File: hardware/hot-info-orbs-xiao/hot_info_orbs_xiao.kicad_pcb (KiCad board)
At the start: 2 copper layers, 198.8 x 45.8 mm, 13 parts, among them SW1 SW_Push, SW2 SW_Push, SW3 SW_Push, U2 XIAO ESP32-S3 Plus

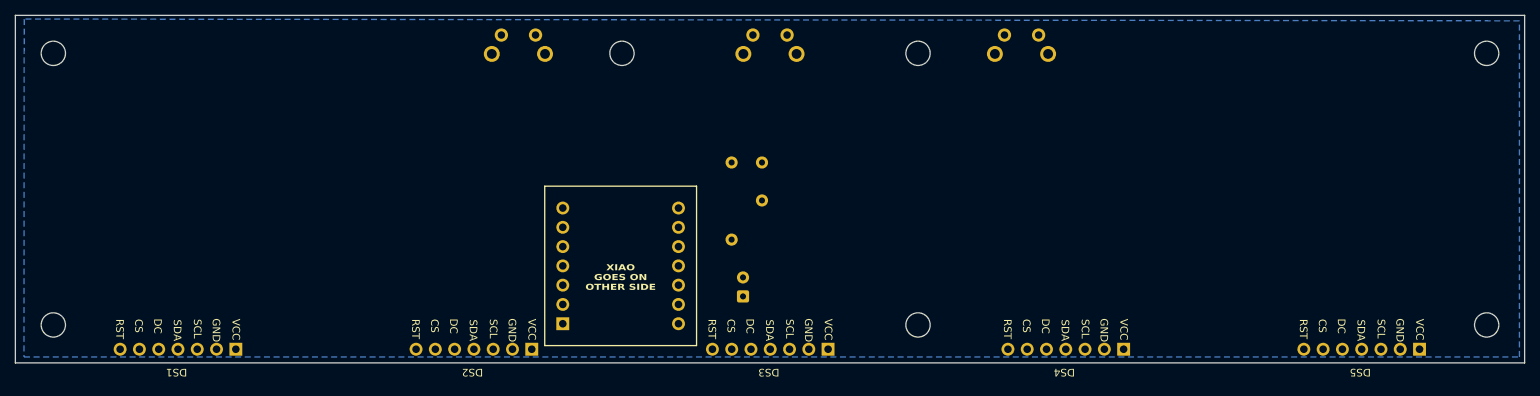
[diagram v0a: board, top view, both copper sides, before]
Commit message: xiao: routed - bottom edge 2 mm lower, 0 errors / 0 unconnected
Freerouting left one connection on every run (SCLK, or DC DS4->DS5) with
the display pin rows 1.8 mm from the bottom edge: nothing could pass under
them. Scott offered a couple of mm at the bottom; 2 mm routes clean in one
pass. Pin rows, parts and holes stay put (bottom holes now 7 mm in).

Rejected first, cheaper but failed:
- GND left to the B.Cu pour instead of tracks: everything else routes, but
  the tracks slice the pour and 6 GND pads end up islanded.
- Reordering nets in the DSN: 12 shuffles, identical result.

route_xiao.py: hole keepouts grown 0.4 mm (two copper_edge_clearance
errors otherwise), and an empty SES is rerun instead of read as "unrouted" -
it is an exit race (docs/TRAPS.md).

DRC with refilled zones: 0 errors, 0 warnings, 0 unconnected, 0 parity.

Co-Authored-By: Claude Opus 5.5 <noreply@anthropic.com>
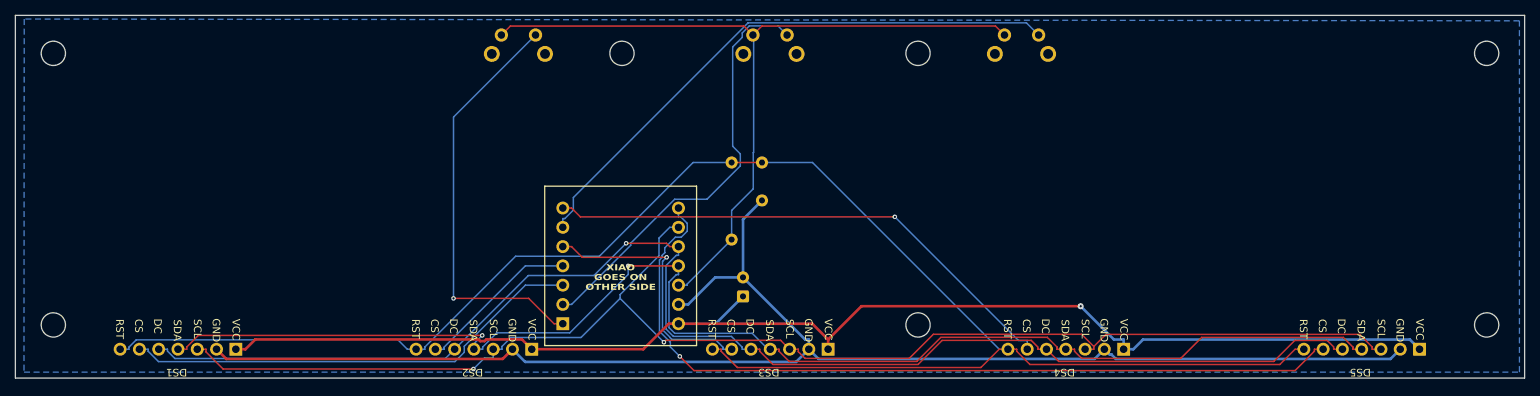
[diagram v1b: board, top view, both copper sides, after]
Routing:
- net /RST: track 0.00 -> 220.6 mm
- net GND: track 0.00 -> 195.0 mm
- net /SCLK: track 0.00 -> 184.0 mm, vias 0 -> 2
- net /DC: track 0.00 -> 183.1 mm, vias 0 -> 1
- net /MOSI: track 0.00 -> 182.4 mm, vias 0 -> 2
- net +5V: track 0.00 -> 176.7 mm, vias 0 -> 1
- net /CS5: track 0.00 -> 110.1 mm, vias 0 -> 1
- net /3V3: track 0.00 -> 106.0 mm
- net /SW3: track 0.00 -> 76.1 mm
- net /CS4: track 0.00 -> 69.6 mm, vias 0 -> 1
- net /CS1: track 0.00 -> 61.2 mm
- net /SW2: track 0.00 -> 56.3 mm
- net /SW1: track 0.00 -> 54.9 mm, vias 0 -> 1
- net /CS3: track 0.00 -> 34.4 mm, vias 0 -> 1
- net /CS2: track 0.00 -> 21.5 mm
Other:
- board size 198.8 x 45.8 mm -> 198.8 x 47.8 mm

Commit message: xiao: club URL on the back, bottom holes 5 mm in, DS labels upright
- handsontech.org under the club name (Scott). The domain, not
  handsontechorg.weebly.com: it is the club's own name for the site and
  301s to weebly, so the silk survives a host change.
- Bottom-row holes follow the 2 mm edge extension down, so all seven are
  5 mm in like the top row. Rejected: keeping them at 7 mm to protect the
  new routing channel - the corners are outside it, and the reroute
  passed with the mid hole lowered: DRC 0/0/0/0, 314 tracks+vias.
- DS1-DS5 front silk set to 0 deg. At 180 (riding the footprint) KiCad
  draws them upright but the STEP export does not, so Fusion showed them
  flipped. Trap recorded.

Co-Authored-By: Claude Opus 5.5 <noreply@anthropic.com>
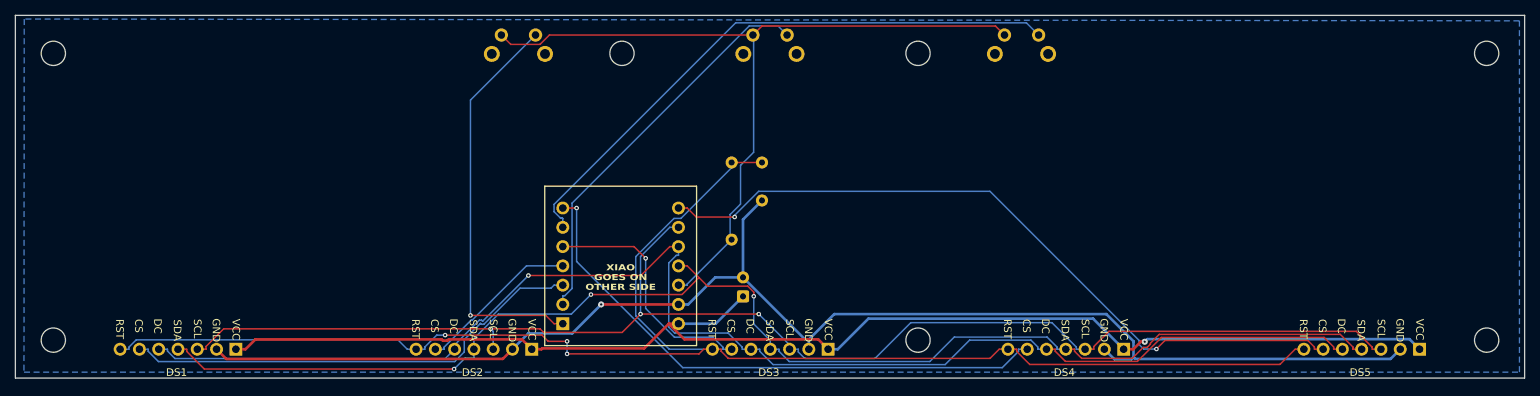
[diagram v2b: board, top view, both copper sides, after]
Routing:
- net /RST: track 220.6 -> 205.2 mm, vias 0 -> 3
- net /CS5: track 110.1 -> 97.0 mm, vias 1 -> 2
- net GND: track 195.0 -> 186.8 mm, vias 0 -> 1
- net /CS4: track 69.6 -> 75.2 mm
- net /SW2: track 56.3 -> 52.5 mm
- net /CS3: track 34.4 -> 31.9 mm
- net /MOSI: track 182.4 -> 180.1 mm, vias 2 -> 3
- net /SW3: track 76.1 -> 78.0 mm
- net /SW1: track 54.9 -> 53.1 mm
- net +5V: track 176.7 -> 175.6 mm
- net /CS1: track 61.2 -> 61.8 mm
- net /SCLK: track 184.0 -> 184.6 mm, vias 2 -> 3
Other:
- outline, holes or cut-outs redrawn
- board text added: "handsontech.org"

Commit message: bom(xiao): Link 1 prices and build-cost total; C1 = 100uF 16V
Prices are the Link 1 listings seen live 2026-10-17, so no +40% estimate
mark. Two totals at the bottom: one build bought in whole packs ($104.50:
5 displays from a 3-pack means two packs), and the per-board share with each
pack pro-rated ($55.58). Kept both because the pack-bought figure alone hugely
overstates a club batch, and the pro-rated one alone hides what the first
board really costs. The XIAO-socket line is 0 in build cost because it comes
out of the display sockets' 60-pack. The PCB is left out of both: a JLCPCB
quote depends on quantity and colors, and guessing it would put an estimate
inside a total that is otherwise measured.

C1 value set by Scott and written into the schematic and PCB Value fields;
kicad-cli BOM shows "100uF 16V", DRC 0/0/0 with schematic parity.

Co-Authored-By: Claude Opus 5.5 <noreply@anthropic.com>
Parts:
- C1: value C_Polarized_Small_US -> 100uF 16V
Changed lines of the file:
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@@
 			)
 		)
-		(property "Value" "C_Polarized_Small_US"
+		(property "Value" "100uF 16V"
 			(at 5.22 4.39 90)
 			(layer "B.Fab")
